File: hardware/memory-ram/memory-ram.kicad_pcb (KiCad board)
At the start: 2 copper layers, 77 x 39 mm, 27 parts, among them J1 Conn_Mem_Ext, J2 Conn_Power, U1 IS61WV5128EDBLL-10TLI, U2 74LVC1G86, U3 MIC5504-3.3YM5, U4 74LVC1G32, U5 74LVC1G332, U6 74LVC1G86, U7 74LVC1G04

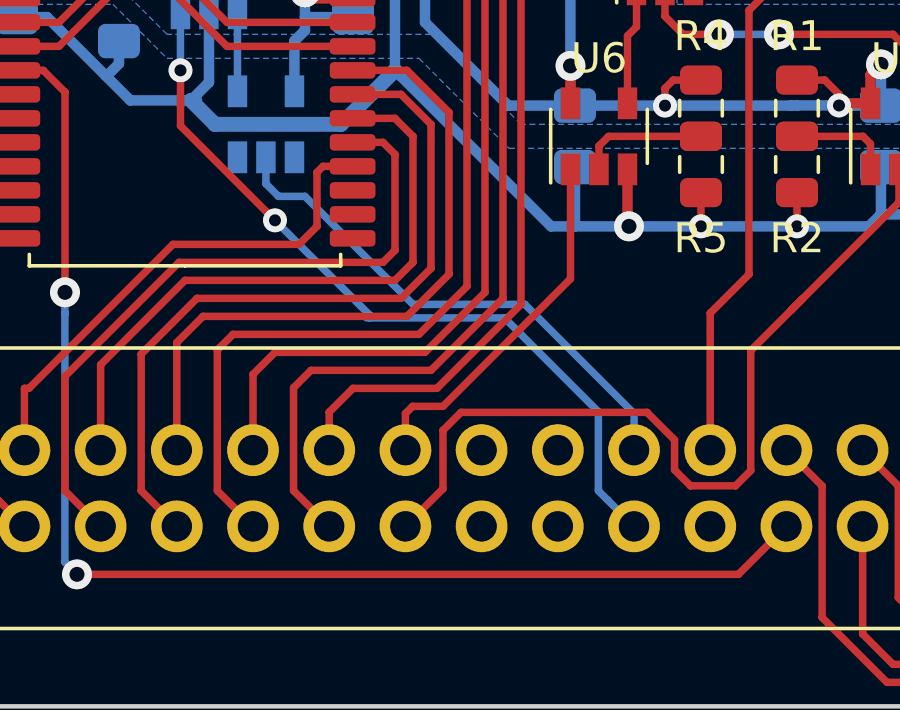
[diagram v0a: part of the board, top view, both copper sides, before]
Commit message: Added ~RESET to memory bus
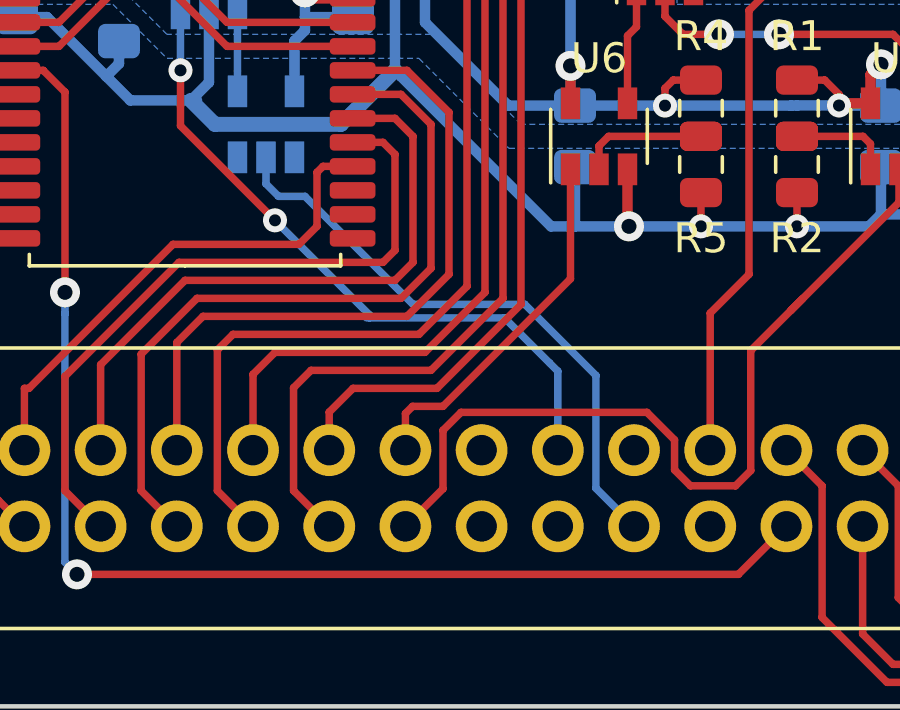
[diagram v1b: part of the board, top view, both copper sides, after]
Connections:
- J1 pad 26: /A24 -> /A30
- J1 pad 27: /A30 -> /A31
- J1 pad 28: /A31 -> Net-(J1-Pad28)
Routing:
- net /A30: track 26.3 -> 22.8 mm
- net /A31: track 17.5 -> 20.1 mm

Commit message: Unified footprints
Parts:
- D1: footprint LED_SMD:LED_0805_2012Metric -> LED_SMD:LED_0805_2012Metric_Pad1.15x1.40mm_HandSolder
- R1, R2, R3, R4, R5: footprint Resistor_SMD:R_0805_2012Metric -> Resistor_SMD:R_0805_2012Metric_Pad1.15x1.40mm_HandSolder
- U2, U3, U4, U6, U7: footprint Package_TO_SOT_SMD:SOT-23-5 -> Package_TO_SOT_SMD:SOT-23-5_HandSoldering
- U5: footprint Package_TO_SOT_SMD:SOT-23-6 -> Package_TO_SOT_SMD:SOT-23-6_Handsoldering
- moved U4 2.30 mm to (110.3, 106.0), turned to 180 degrees
- moved C5 1.38 mm to (110.3, 106.0)
- moved C8 1.23 mm to (120.8, 114.0)
- moved U7 1.16 mm to (98.0, 114.8)
- moved U3 0.53 mm to (124.7, 114.0)
- moved R1 0.09 mm to (115.8, 113.0)
- moved R2 0.09 mm to (115.8, 115.0)
- moved R4 0.09 mm to (112.6, 113.0)
- moved R5 0.09 mm to (112.6, 115.0)
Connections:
- net Net-(J1-Pad28) renamed /~RESET
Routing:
- net GND: track 154.3 -> 171.9 mm
- net /A30: track 22.8 -> 30.8 mm
- net /A19-20: track 18.6 -> 13.9 mm
- net /X20: track 3.92 -> 6.64 mm
- net /V_IN: track 18.5 -> 16.3 mm
- net /X19: track 11.5 -> 13.4 mm
- net VCC: track 94.3 -> 95.8 mm
- net /~MEM_OE: track 46.7 -> 47.4 mm
- net /~A31: track 2.70 -> 3.31 mm
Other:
- board text added: "2020-06-11"
- board text removed: "2020-05-30"
